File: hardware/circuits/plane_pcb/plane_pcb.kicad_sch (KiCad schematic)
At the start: 32 parts, among them J1 J1, J2 J2, J3 J3, J4 J4, U1 Magnetometer_Breakout, U2 U1

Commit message: update to smd components
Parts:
- R16, R17, R18, R19, R20, R21, R3, R4, R5, R6, R7, R8: footprint Resistor_THT:R_Axial_DIN0207_L6.3mm_D2.5mm_P10.16mm_Horizontal -> Resistor_SMD:R_1206_3216Metric_Pad1.30x1.75mm_HandSolder
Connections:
- net 3V3: now also lora1.17 (3V3); no longer Power1.1 (Pin_1)
- net 5V: now also Power1.1 (Pin_1)
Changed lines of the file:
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@@
 	(wire
 		(pts
+			(xy 38.1 168.91) (xy 45.72 168.91)
+		)
+		(stroke
+			(width 0)
+			(type default)
+		)
+	)
+	(wire
+		(pts
 			(xy 132.08 55.88) (xy 137.16 55.88)
 		)
@@
 		)
 	)
+	(label "3V3"
+		(at 38.1 168.91 0)
+		(effects
+			(font
+				(size 1.27 1.27)
+			)
+			(justify left bottom)
+		)
+	)
 	(label "UART_RX"
 		(at 137.16 55.88 0)
@@
 		)
 	)
-	(label "3V3"
+	(label "5V"
 		(at 99.06 127 0)
 		(effects
@@
 			)
 		)
-		(property "Footprint" "Resistor_THT:R_Axial_DIN0207_L6.3mm_D2.5mm_P10.16mm_Horizontal"
+		(property "Footprint" "Resistor_SMD:R_1206_3216Metric_Pad1.30x1.75mm_HandSolder"
 			(at 198.12 221.742 90)
 			(hide yes)
@@
 			)
 		)
-		(property "Footprint" "Resistor_THT:R_Axial_DIN0207_L6.3mm_D2.5mm_P10.16mm_Horizontal"
+		(property "Footprint" "Resistor_SMD:R_1206_3216Metric_Pad1.30x1.75mm_HandSolder"
 			(at 173.228 233.68 90)
 			(hide yes)
@@
 			)
 		)
-		(property "Footprint" "Resistor_THT:R_Axial_DIN0207_L6.3mm_D2.5mm_P10.16mm_Horizontal"
+		(property "Footprint" "Resistor_SMD:R_1206_3216Metric_Pad1.30x1.75mm_HandSolder"
 			(at 83.82 73.66 0)
 			(hide yes)
@@
 			)
 		)
-		(property "Footprint" "Resistor_THT:R_Axial_DIN0207_L6.3mm_D2.5mm_P10.16mm_Horizontal"
+		(property "Footprint" "Resistor_SMD:R_1206_3216Metric_Pad1.30x1.75mm_HandSolder"
 			(at 85.09 80.01 0)
 			(hide yes)
@@
 			)
 		)
-		(property "Footprint" "Resistor_THT:R_Axial_DIN0207_L6.3mm_D2.5mm_P10.16mm_Horizontal"
+		(property "Footprint" "Resistor_SMD:R_1206_3216Metric_Pad1.30x1.75mm_HandSolder"
 			(at 154.94 216.662 90)
 			(hide yes)
@@
 			)
 		)
-		(property "Footprint" "Resistor_THT:R_Axial_DIN0207_L6.3mm_D2.5mm_P10.16mm_Horizontal"
+		(property "Footprint" "Resistor_SMD:R_1206_3216Metric_Pad1.30x1.75mm_HandSolder"
 			(at 194.818 236.22 90)
 			(hide yes)
@@
 			)
 		)
-		(property "Description" ""
+		(property "Description" "Heltec WiFi LoRa 32 V3.2 dev board (ESP32-S3 + SX1262), 36-pin dual header"
 			(at 58.42 149.86 0)
+			(hide yes)
 			(show_name no)
 			(do_not_autoplace no)
@@
 			)
 		)
-		(property "Footprint" "Resistor_THT:R_Axial_DIN0207_L6.3mm_D2.5mm_P10.16mm_Horizontal"
+		(property "Footprint" "Resistor_SMD:R_1206_3216Metric_Pad1.30x1.75mm_HandSolder"
 			(at 151.638 231.14 90)
 			(hide yes)
@@
 			)
 		)
-		(property "Footprint" "Resistor_THT:R_Axial_DIN0207_L6.3mm_D2.5mm_P10.16mm_Horizontal"
+		(property "Footprint" "Resistor_SMD:R_1206_3216Metric_Pad1.30x1.75mm_HandSolder"
 			(at 132.08 66.04 0)
 			(hide yes)
@@
 			)
 		)
-		(property "Footprint" "Resistor_THT:R_Axial_DIN0207_L6.3mm_D2.5mm_P10.16mm_Horizontal"
+		(property "Footprint" "Resistor_SMD:R_1206_3216Metric_Pad1.30x1.75mm_HandSolder"
 			(at 119.38 44.45 0)
 			(hide yes)
@@
 			)
 		)
-		(property "Footprint" "Resistor_THT:R_Axial_DIN0207_L6.3mm_D2.5mm_P10.16mm_Horizontal"
+		(property "Footprint" "Resistor_SMD:R_1206_3216Metric_Pad1.30x1.75mm_HandSolder"
 			(at 29.21 78.74 0)
 			(hide yes)
@@
 			)
 		)
-		(property "Footprint" "Resistor_THT:R_Axial_DIN0207_L6.3mm_D2.5mm_P10.16mm_Horizontal"
+		(property "Footprint" "Resistor_SMD:R_1206_3216Metric_Pad1.30x1.75mm_HandSolder"
 			(at 26.67 86.36 0)
 			(hide yes)
@@
 			)
 		)
-		(property "Footprint" "Resistor_THT:R_Axial_DIN0207_L6.3mm_D2.5mm_P10.16mm_Horizontal"
+		(property "Footprint" "Resistor_SMD:R_1206_3216Metric_Pad1.30x1.75mm_HandSolder"
 			(at 176.53 219.202 90)
 			(hide yes)

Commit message: finish pcb rework with smd components
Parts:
- C1, C2, C3: footprint Capacitor_THT:C_Disc_D5.0mm_W2.5mm_P5.00mm -> Capacitor_SMD:C_1206_3216Metric_Pad1.33x1.80mm_HandSolder
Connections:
- net GND_MAIN: now also lora1.18 (GND)
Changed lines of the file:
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@@
 	(wire
 		(pts
+			(xy 35.56 171.45) (xy 45.72 171.45)
+		)
+		(stroke
+			(width 0)
+			(type default)
+		)
+	)
+	(wire
+		(pts
 			(xy 181.61 243.84) (xy 193.04 243.84)
 		)
@@
 		)
 	)
+	(label "GND_MAIN"
+		(at 35.56 171.45 0)
+		(effects
+			(font
+				(size 1.27 1.27)
+			)
+			(justify left bottom)
+		)
+	)
 	(symbol
 		(lib_id "power:PWR_FLAG")
@@
 			)
 		)
-		(property "Footprint" "Capacitor_THT:C_Disc_D5.0mm_W2.5mm_P5.00mm"
+		(property "Footprint" "Capacitor_SMD:C_1206_3216Metric_Pad1.33x1.80mm_HandSolder"
 			(at 160.9852 234.95 0)
 			(hide yes)
@@
 			)
 		)
-		(property "Footprint" "Capacitor_THT:C_Disc_D5.0mm_W2.5mm_P5.00mm"
+		(property "Footprint" "Capacitor_SMD:C_1206_3216Metric_Pad1.33x1.80mm_HandSolder"
 			(at 204.1652 240.03 0)
 			(hide yes)
@@
 			)
 		)
-		(property "Footprint" "Capacitor_THT:C_Disc_D5.0mm_W2.5mm_P5.00mm"
+		(property "Footprint" "Capacitor_SMD:C_1206_3216Metric_Pad1.33x1.80mm_HandSolder"
 			(at 182.5752 237.49 0)
 			(hide yes)

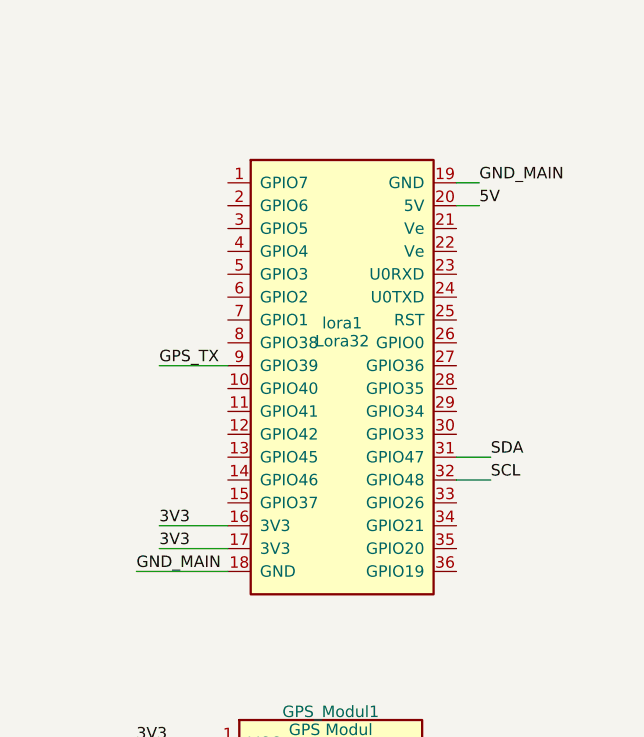
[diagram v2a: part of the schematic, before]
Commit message: fix pcb and arduino nano pinout
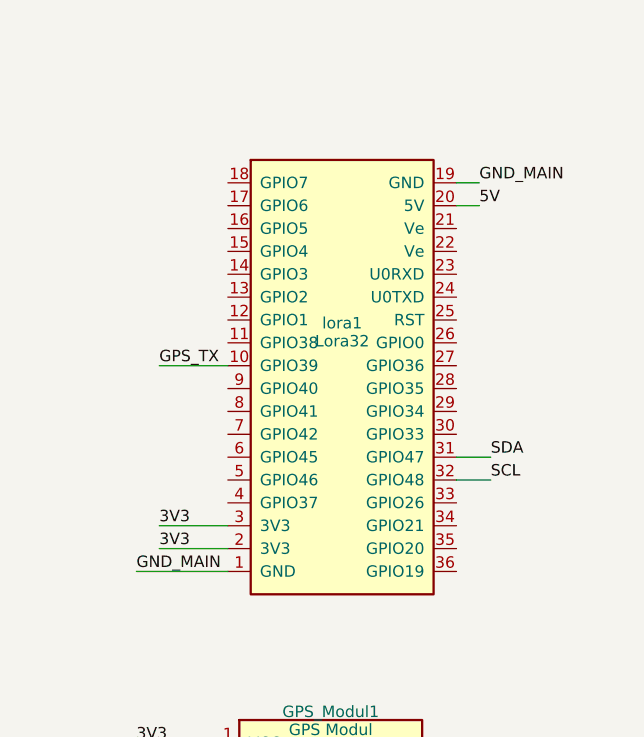
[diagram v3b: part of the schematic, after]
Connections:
- net 3V3: now also lora1.2 (3V3), lora1.3 (3V3); no longer lora1.16 (3V3), lora1.17 (3V3)
- net GND_MAIN: now also lora1.1 (GND); no longer lora1.18 (GND)
- net GPS_TX: now also lora1.10 (GPIO39); no longer lora1.9 (GPIO39)

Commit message: fix last pcb mistakes (hopefully) Rev1.0_2
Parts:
- ADS1115: footprint Connector_PinHeader_2.54mm:PinHeader_1x11_P2.54mm_Vertical -> Connector_PinHeader_2.54mm:PinHeader_1x10_P2.54mm_Vertical
- Arduino_Nano1: footprint Module:Arduino_Nano -> auto_flight:Arduino_Nano
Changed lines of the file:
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@@
 			)
 		)
-		(property "Footprint" "Connector_PinHeader_2.54mm:PinHeader_1x11_P2.54mm_Vertical"
+		(property "Footprint" "Connector_PinHeader_2.54mm:PinHeader_1x10_P2.54mm_Vertical"
 			(at 123.19 220.98 0)
 			(hide yes)
@@
 			)
 		)
-		(property "Footprint" "Module:Arduino_Nano"
+		(property "Footprint" "auto_flight:Arduino_Nano"
 			(at 58.42 50.8 0)
 			(hide yes)

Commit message: fix battery percentage measurement
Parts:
- R16, R18, R20: value 33k -> 47k
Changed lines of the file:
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@@
 			)
 		)
-		(property "Value" "33k"
+		(property "Value" "47k"
 			(at 173.99 234.9499 0)
 			(show_name no)
@@
 			)
 		)
-		(property "Value" "33k"
+		(property "Value" "47k"
 			(at 195.58 237.4899 0)
 			(show_name no)
@@
 			)
 		)
-		(property "Value" "33k"
+		(property "Value" "47k"
 			(at 152.4 232.4099 0)
 			(show_name no)

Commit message: fix pcb voltage divider
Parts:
- R16, R18, R20: value 47k -> 10k
- R17, R19, R21: value 10k -> 47k
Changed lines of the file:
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@@
 			)
 		)
-		(property "Value" "10k"
+		(property "Value" "47k"
 			(at 198.12 219.71 90)
 			(show_name no)
@@
 			)
 		)
-		(property "Value" "47k"
+		(property "Value" "10k"
 			(at 173.99 234.9499 0)
 			(show_name no)
@@
 			)
 		)
-		(property "Value" "10k"
+		(property "Value" "47k"
 			(at 154.94 214.63 90)
 			(show_name no)
@@
 			)
 		)
-		(property "Value" "47k"
+		(property "Value" "10k"
 			(at 195.58 237.4899 0)
 			(show_name no)
@@
 			)
 		)
-		(property "Value" "47k"
+		(property "Value" "10k"
 			(at 152.4 232.4099 0)
 			(show_name no)
@@
 			)
 		)
-		(property "Value" "10k"
+		(property "Value" "47k"
 			(at 176.53 217.17 90)
 			(show_name no)
